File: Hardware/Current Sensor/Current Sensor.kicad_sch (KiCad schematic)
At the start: 5 parts, among them J1 Screw_Terminal_01x02, J2 Conn_01x03, U1 INA240A1D

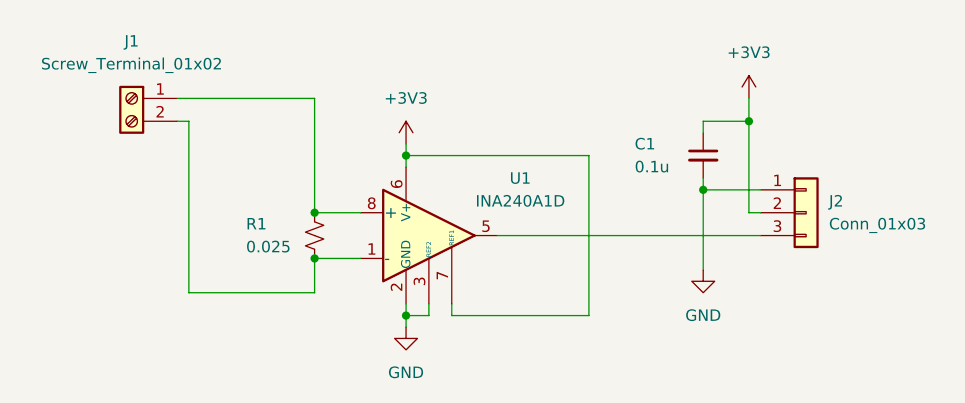
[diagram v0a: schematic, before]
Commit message: 
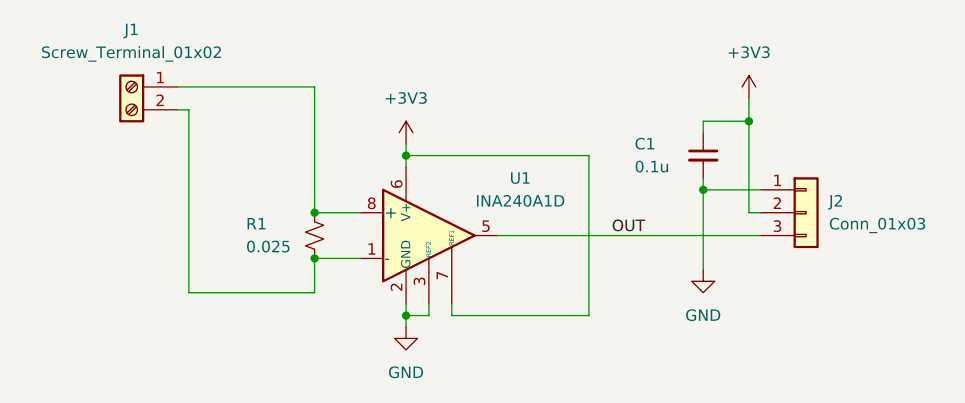
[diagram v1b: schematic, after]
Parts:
- J1: footprint (none) -> TerminalBlock_Phoenix:TerminalBlock_Phoenix_PT-1,5-2-3.5-H_1x02_P3.50mm_Horizontal
- J2: footprint (none) -> Connector_PinHeader_2.54mm:PinHeader_1x03_P2.54mm_Vertical
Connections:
- net OUT: now reaches J2.3 (Pin_3), U1.5
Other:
- moved on the sheet: J1
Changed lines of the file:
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@@
-    (stroke (width 0) (type default) (color 0 0 0 0))
-  )
-  (wire (pts (xy 43.18 39.37) (xy 58.42 39.37))
     (stroke (width 0) (type default) (color 0 0 0 0))
   )
@@
     (stroke (width 0) (type default) (color 0 0 0 0))
   )
+  (wire (pts (xy 43.18 38.1) (xy 58.42 38.1))
+    (stroke (width 0) (type default) (color 0 0 0 0))
+  )
+  (wire (pts (xy 43.18 40.64) (xy 44.45 40.64))
+    (stroke (width 0) (type default) (color 0 0 0 0))
+  )
   (wire (pts (xy 106.68 52.07) (xy 107.95 52.07))
     (stroke (width 0) (type default) (color 0 0 0 0))
@@
     (stroke (width 0) (type default) (color 0 0 0 0))
   )
-  (wire (pts (xy 44.45 41.91) (xy 44.45 60.96))
+  (wire (pts (xy 44.45 40.64) (xy 44.45 60.96))
     (stroke (width 0) (type default) (color 0 0 0 0))
   )
@@
     (stroke (width 0) (type default) (color 0 0 0 0))
   )
-  (wire (pts (xy 58.42 39.37) (xy 58.42 52.07))
-    (stroke (width 0) (type default) (color 0 0 0 0))
-  )
-  (wire (pts (xy 44.45 41.91) (xy 43.18 41.91))
+  (wire (pts (xy 58.42 38.1) (xy 58.42 52.07))
     (stroke (width 0) (type default) (color 0 0 0 0))
   )
@@
   (wire (pts (xy 101.6 48.26) (xy 101.6 49.53))
     (stroke (width 0) (type default) (color 0 0 0 0))
+  )
+  (label "OUT" (at 91.44 54.61 0)
+    (effects (font (size 1.27 1.27)) (justify left bottom))
   )
   (symbol (lib_id "power:+3V3") (at 68.58 44.45 0) (unit 1)
@@
       (effects (font (size 1.27 1.27)) (justify left))
     )
-    (property "Footprint" "" (id 2) (at 113.03 52.07 0)
+    (property "Footprint" "Connector_PinHeader_2.54mm:PinHeader_1x03_P2.54mm_Vertical" (id 2) (at 113.03 52.07 0)
       (effects (font (size 1.27 1.27)) hide)
     )
@@
     (pin "2")
   )
-  (symbol (lib_id "Connector:Screw_Terminal_01x02") (at 38.1 39.37 0) (mirror y) (unit 1)
-    (in_bom yes) (on_board yes) (fields_autoplaced)
-    (property "Reference" "J1" (id 0) (at 38.1 33.02 0))
-    (property "Value" "Screw_Terminal_01x02" (id 1) (at 38.1 35.56 0))
-    (property "Footprint" "" (id 2) (at 38.1 39.37 0)
-      (effects (font (size 1.27 1.27)) hide)
-    )
-    (property "Datasheet" "~" (id 3) (at 38.1 39.37 0)
+  (symbol (lib_id "Connector:Screw_Terminal_01x02") (at 38.1 38.1 0) (mirror y) (unit 1)
+    (in_bom yes) (on_board yes) (fields_autoplaced)
+    (property "Reference" "J1" (id 0) (at 38.1 31.75 0))
+    (property "Value" "Screw_Terminal_01x02" (id 1) (at 38.1 34.29 0))
+    (property "Footprint" "TerminalBlock_Phoenix:TerminalBlock_Phoenix_PT-1,5-2-3.5-H_1x02_P3.50mm_Horizontal" (id 2) (at 38.1 38.1 0)
+      (effects (font (size 1.27 1.27)) hide)
+    )
+    (property "Datasheet" "~" (id 3) (at 38.1 38.1 0)
       (effects (font (size 1.27 1.27)) hide)
     )
@@
     )
     (path "/fcd7ba4a-ccab-4ad5-9aba-4c762e653eeb"
-      (reference "J1") (unit 1) (value "Screw_Terminal_01x02") (footprint "TerminalBlock:TerminalBlock_Altech_AK300-2_P5.00mm")
+      (reference "J1") (unit 1) (value "Screw_Terminal_01x02") (footprint "TerminalBlock_Phoenix:TerminalBlock_Phoenix_PT-1,5-2-3.5-H_1x02_P3.50mm_Horizontal")
     )
     (path "/32479e0c-4f64-4d51-9ef0-2ead649e178c"
-      (reference "J2") (unit 1) (value "Conn_01x03") (footprint "Connector_PinHeader_2.54mm:PinHeader_1x03_P2.54mm_Horizontal")
+      (reference "J2") (unit 1) (value "Conn_01x03") (footprint "Connector_PinHeader_2.54mm:PinHeader_1x03_P2.54mm_Vertical")
     )
     (path "/d035ac68-791d-4ce8-ae26-2e6d38691105"
